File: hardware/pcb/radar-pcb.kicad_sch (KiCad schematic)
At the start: 66 parts, among them J1 USB-C zasilanie 5 V (GCT USB4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, J10 Awaryjne wgrywanie: RST GND B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, J2 DevKit J1, J3 DevKit J3, J4 HC-SR04 (kabel): VCC TRIG ECH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, J5 Serwo SG90 (kabel): GND +5V S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, J6 MAX7219 Elegoo: VCC GND DIN C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, J7 OLED SH1106: VCC GND SCK SDA, J8 Buzzer: + -, J9 Przycisk zewnetrzny, Q2 MMBT3904, SW1 Przycisk ON/standby (katowy), U1 SN74AHCT125D, U2 AP22804AW5 (przelacznik 5 V, 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

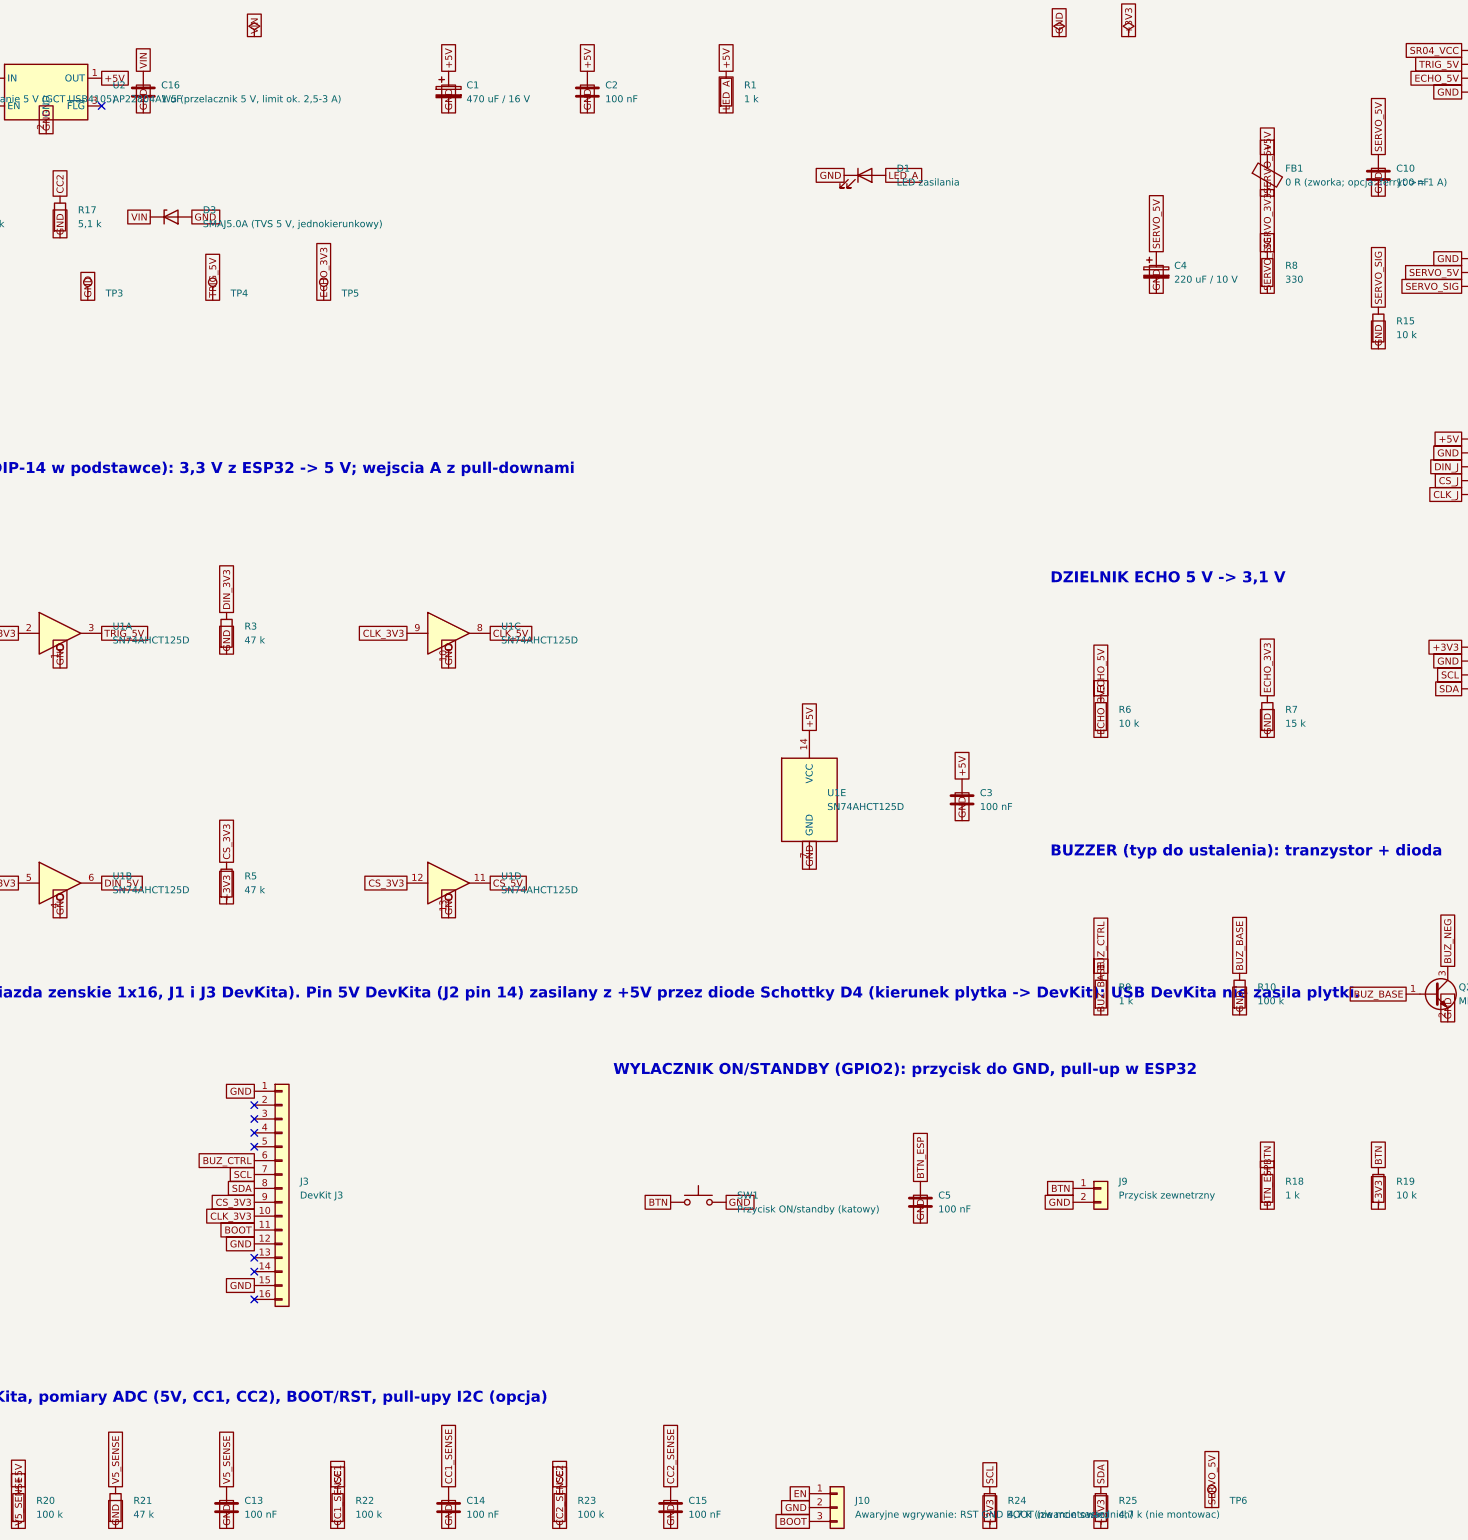
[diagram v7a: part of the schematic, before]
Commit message: PCB: second audit (U2 next to USB-C, J10 near RST/BOOT, FLG to GPIO23), docs and renders
Co-Authored-By: Claude Sonnet 5.5 <noreply@anthropic.com>
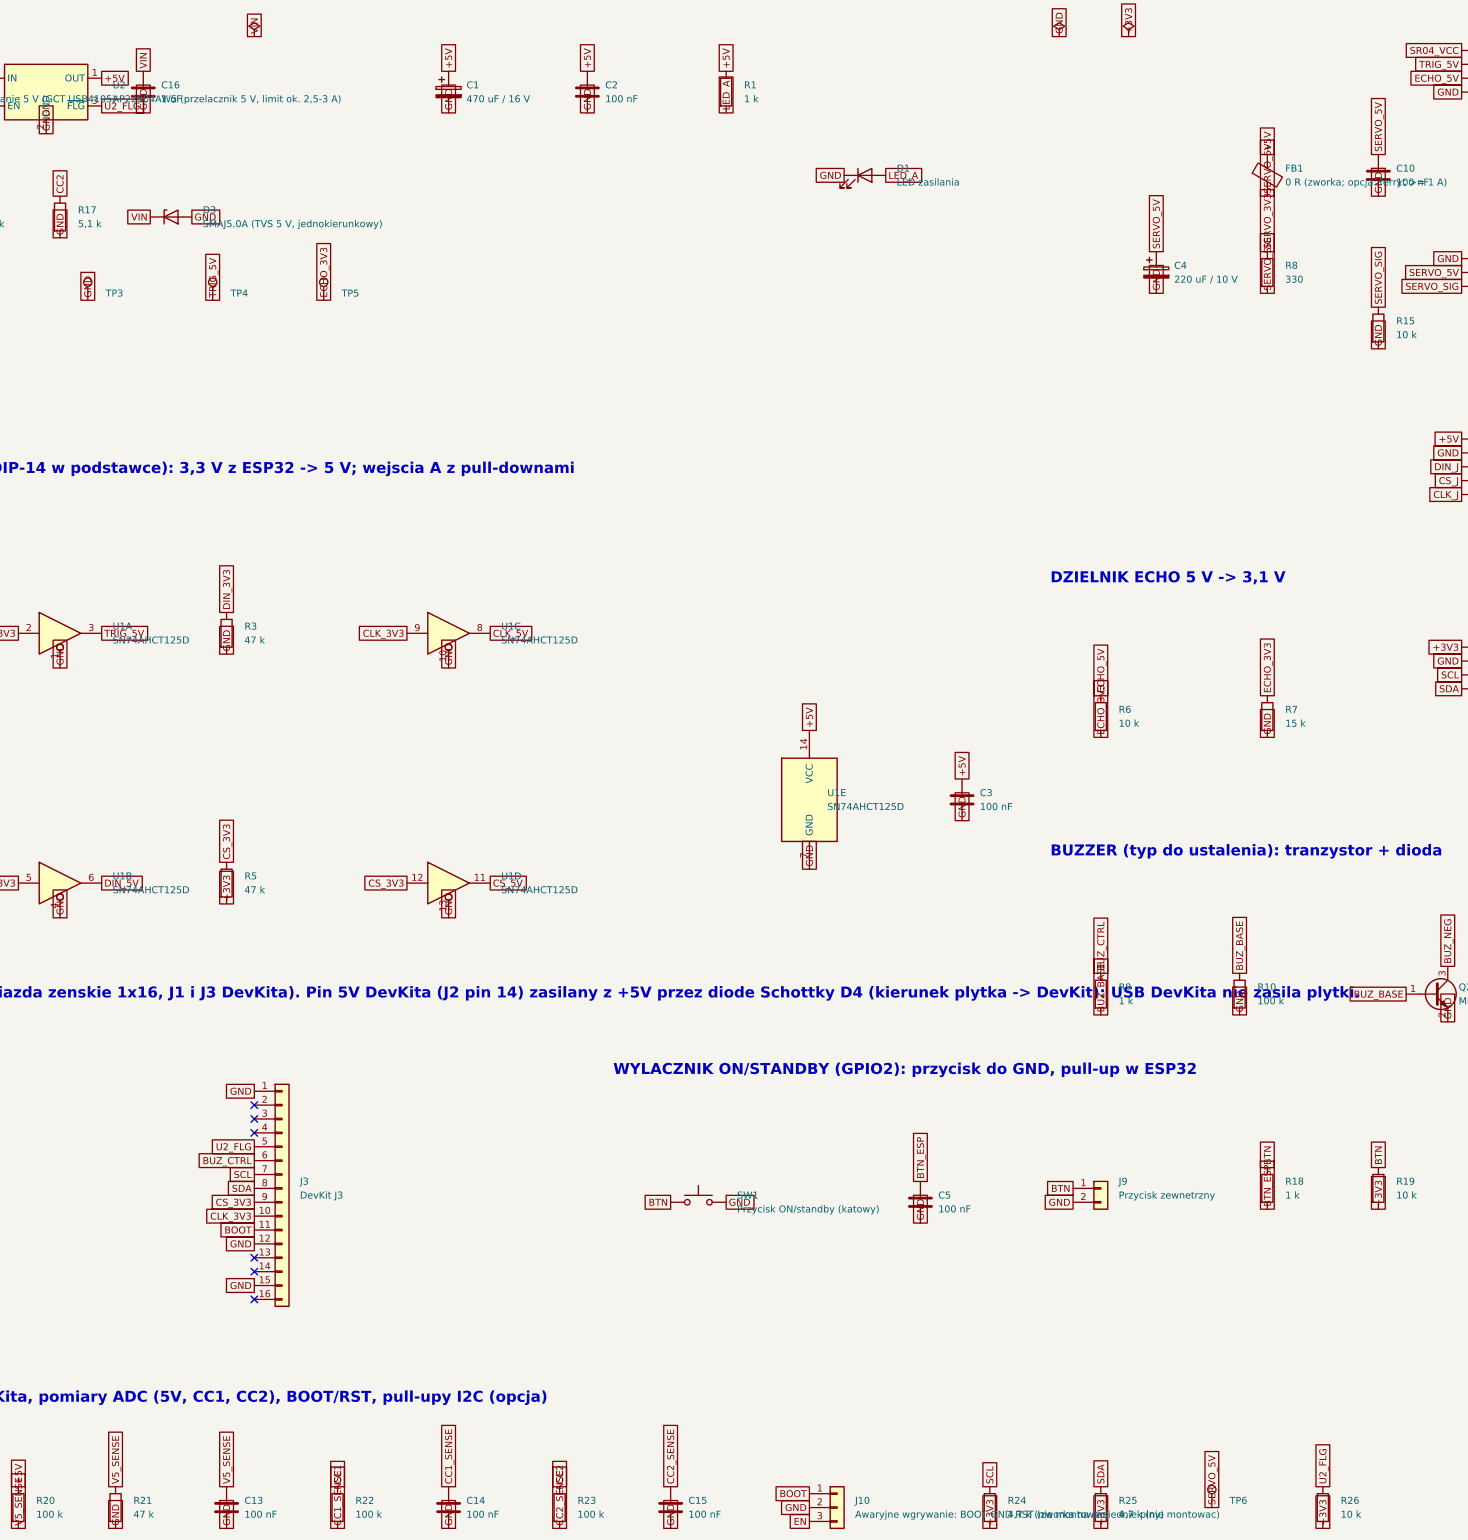
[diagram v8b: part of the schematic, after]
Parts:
- added R26: 10 k, Resistor_SMD:R_0805_2012Metric, symbol Device:R
- J10: value Awaryjne wgrywanie: RST GND BOOT (zwarcie sasiednich) -> Awaryjne wgrywanie: BOOT GND RST (zworka na sasiednie piny)
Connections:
- net +3V3: now also R26.2
- net BOOT: now also J10.1 (Pin_1); no longer J10.3 (Pin_3)
- net EN: now also J10.3 (Pin_3); no longer J10.1 (Pin_1)
- net U2_FLG: now reaches J3.5 (Pin_5)
- net U2_FLG: now also U2.3 (~{FLG}), R26.1
- no-connect marks 18 -> 16
